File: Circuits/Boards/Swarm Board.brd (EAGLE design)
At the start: 76.2 x 76.2 mm, 83 parts, among them CON1 ISP(2X3), T1 NPN2N2222, T10 TEFT4300, T11 NPN2N2222, T12 NPN2N2222, T2 NPN2N2222, T3 NPN2N2222, T4 TEFT4300, T5 TEFT4300, T6 TEFT4300, T7 TEFT4300, T8 TEFT4300, T9 TEFT4300, U1 ATMEGA324P, U2 MCP73832SOT-23, U3 TB6552FN/FNG

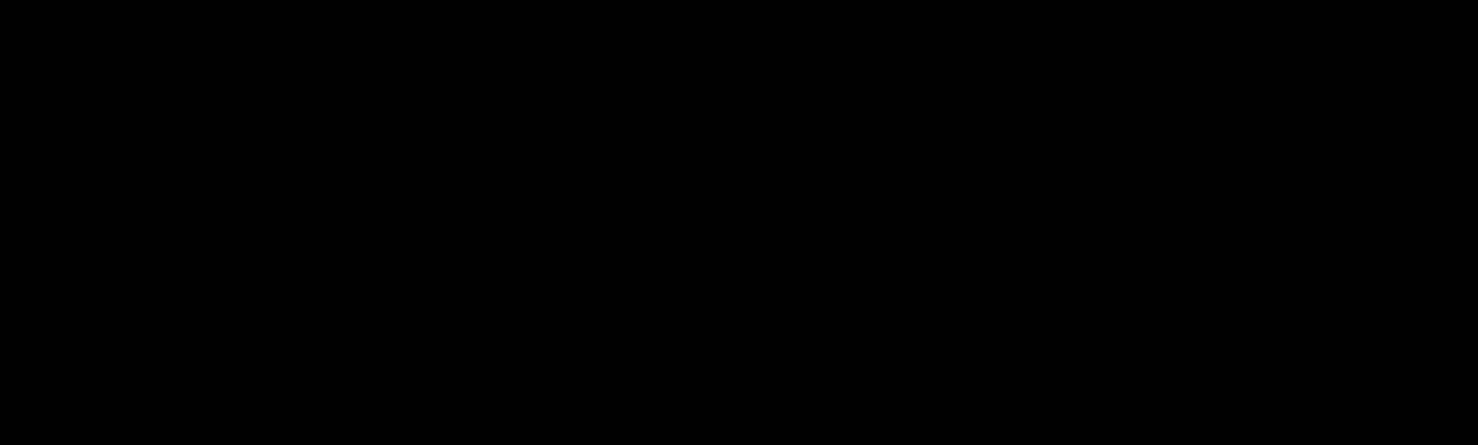
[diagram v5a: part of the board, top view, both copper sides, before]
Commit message: 
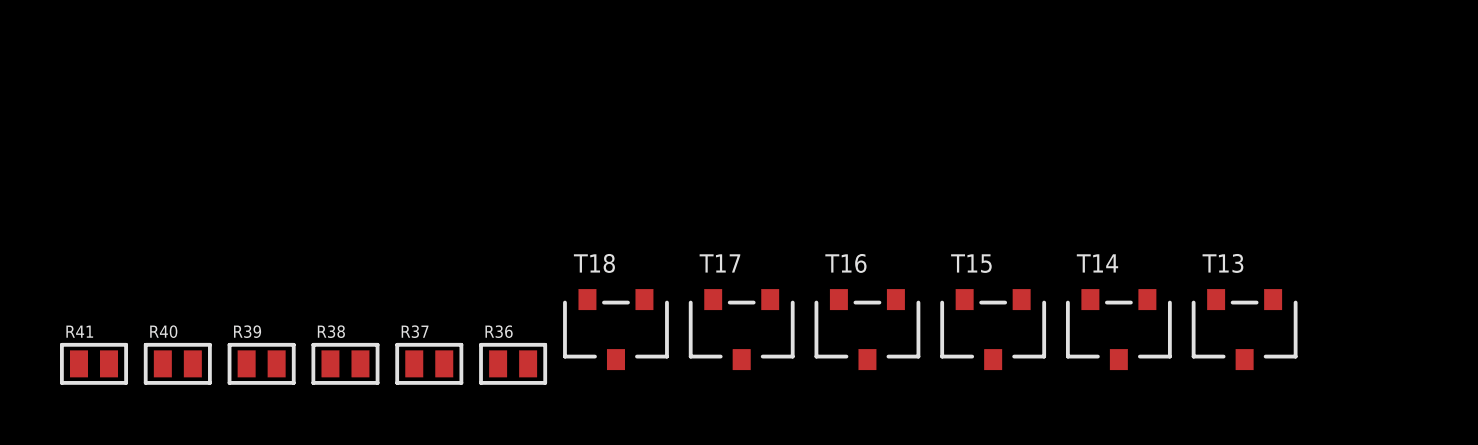
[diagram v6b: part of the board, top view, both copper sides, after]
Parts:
- added R36, R37, R38, R39, R40, R41: (no value), Passive:0603
- added T13, T14, T15, T16, T17, T18: NPN2N2222, Passive:SOT23
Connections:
- removed net BL: R20.2, T7.2
- removed net BM: R21.2, T8.2
- removed net BR: R24.2, T9.2
- removed net FL: R17.2, T4.2
- removed net FM: R18.2, T5.2
- removed net FR: R19.2, T6.2
- new net N$27: R17.1, T13.1, T4.1
- new net N$28: R36.1, T13.3
- new net N$29: R37.1, T14.3
- new net N$30: R38.1, T15.3
- new net N$31: R39.1, T16.3
- new net N$32: R40.1, T17.3
- new net N$33: R41.1, T18.3
- new net N$34: R24.1, T18.1, T9.1
- new net N$35: R21.1, T17.1, T8.1
- new net N$36: R20.1, T16.1, T7.1
- new net N$37: R19.1, T15.1, T6.1
- new net N$38: R18.1, T14.1, T5.1
- net +3V: now also R17.2, R18.2, R19.2, R20.2, R21.2, R24.2, R36.2, R37.2, R38.2, R39.2, R40.2, R41.2; no longer T4.1, T5.1, T6.1, T7.1, T8.1, T9.1
- net GND: now also T13.2, T14.2, T15.2, T16.2, T17.2, T18.2, T4.2, T5.2, T6.2, T7.2, T8.2, T9.2; no longer R17.1, R18.1, R19.1, R20.1, R21.1, R24.1

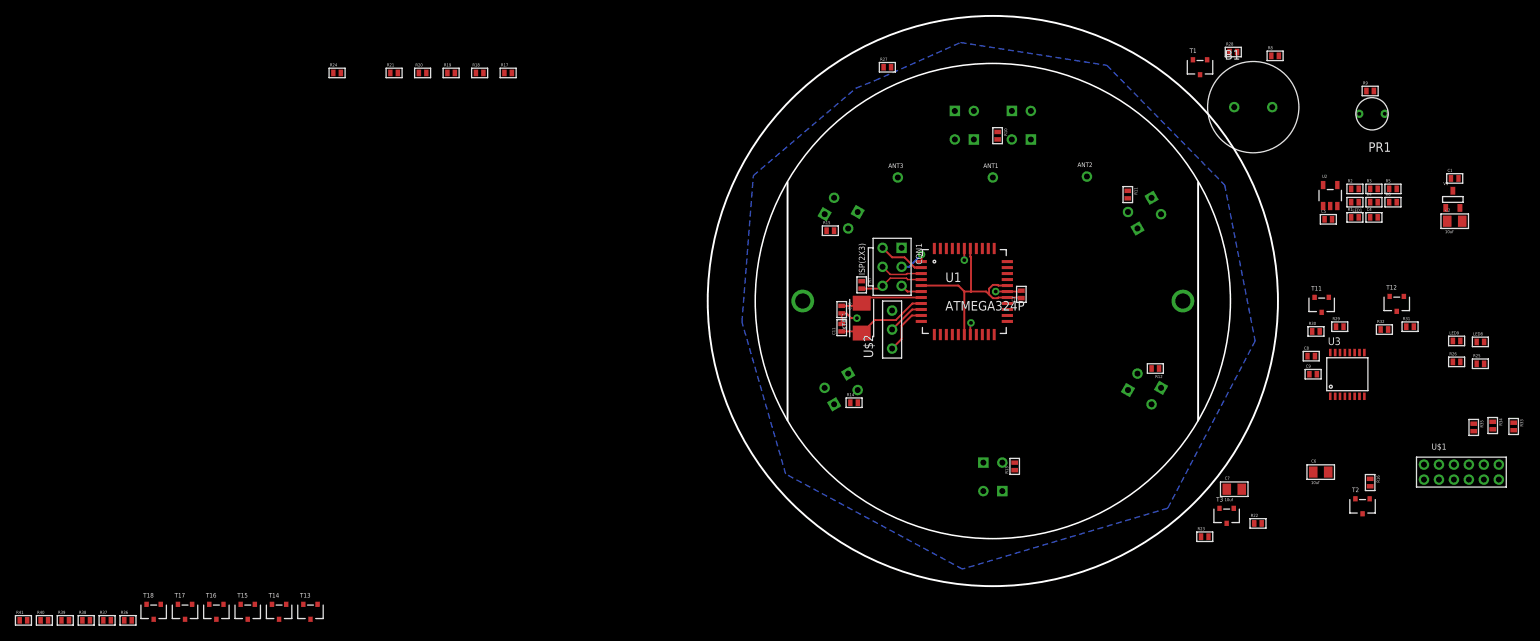
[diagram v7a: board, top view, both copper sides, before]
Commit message: 
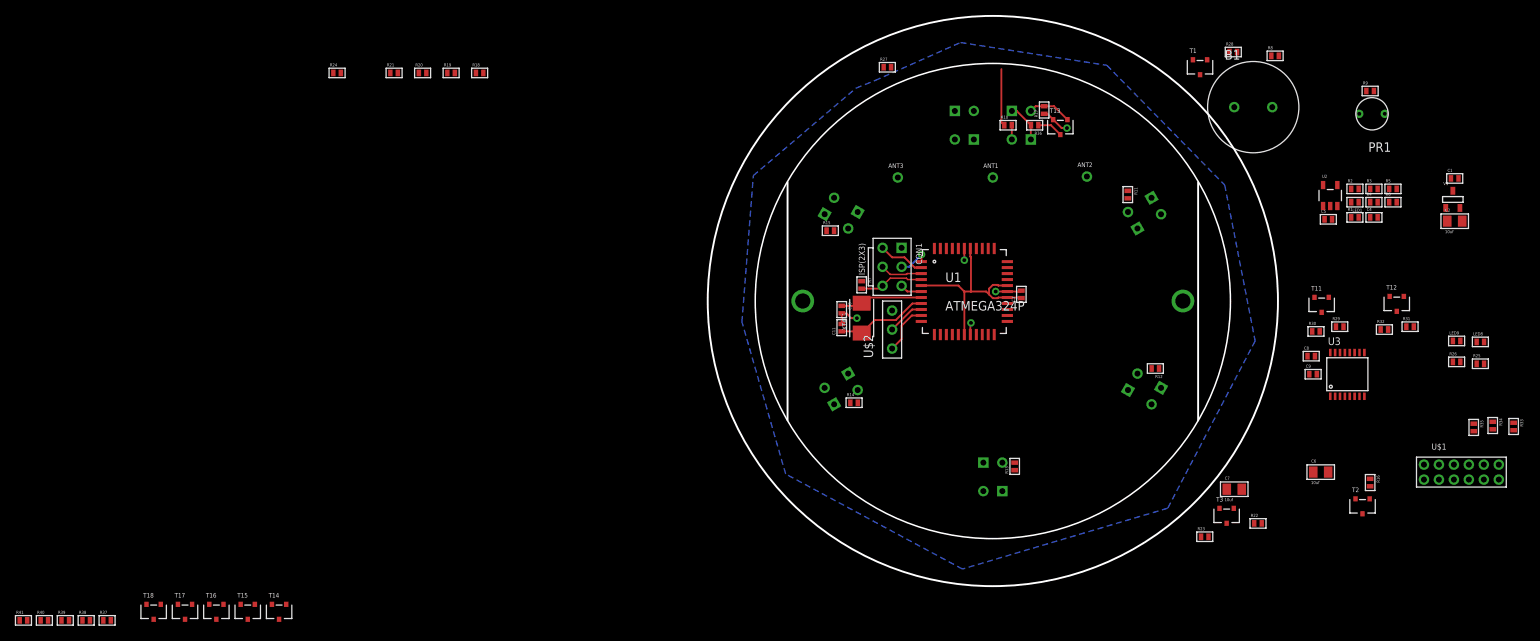
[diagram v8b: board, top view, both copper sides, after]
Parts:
- moved R36 138.0 mm to (37.3, 55.2), turned to 180 degrees
- moved T13 119.3 mm to (40.8, 55.0)
- moved R17 71.8 mm to (38.6, 57.3), turned to 90 degrees
- moved R10 1.98 mm to (33.8, 55.2), turned to 0 degrees
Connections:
- net +3V: now also T4.1, T5.1, T6.1, T7.1, T8.1, T9.1; no longer R17.2, R18.2, R19.2, R20.2, R21.2, R24.2
- net GND: now also R17.1, R18.1, R19.1, R20.1, R21.1, R24.1; no longer T4.2, T5.2, T6.2, T7.2, T8.2, T9.2
- net N$27: now also R17.2, T4.2; no longer R17.1, T4.1
- net N$34: now also R24.2, T9.2; no longer R24.1, T9.1
- net N$35: now also R21.2, T8.2; no longer R21.1, T8.1
- net N$36: now also R20.2, T7.2; no longer R20.1, T7.1
- net N$37: now also R19.2, T6.2; no longer R19.1, T6.1
- net N$38: now also R18.2, T5.2; no longer R18.1, T5.1
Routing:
- net N$10: track 0.00 -> 7.66 mm
- net N$27: track 0.00 -> 5.89 mm
- net +3V: track 29.1 -> 34.4 mm
- net GND: track 13.3 -> 17.1 mm, vias 4 -> 5
- net N$28: track 0.00 -> 3.45 mm
- net N$13: track 0.00 -> 1.91 mm
